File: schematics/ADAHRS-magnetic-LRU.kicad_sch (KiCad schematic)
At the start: 23 parts, among them Q1 2N2222, Q2 IRF7171M, Q3 Q2 - 2N2907, Q4 2N2222, Q5 IRF7171M, U2 AD8421TRMZ-EP, U3 AD8421TRMZ-EP

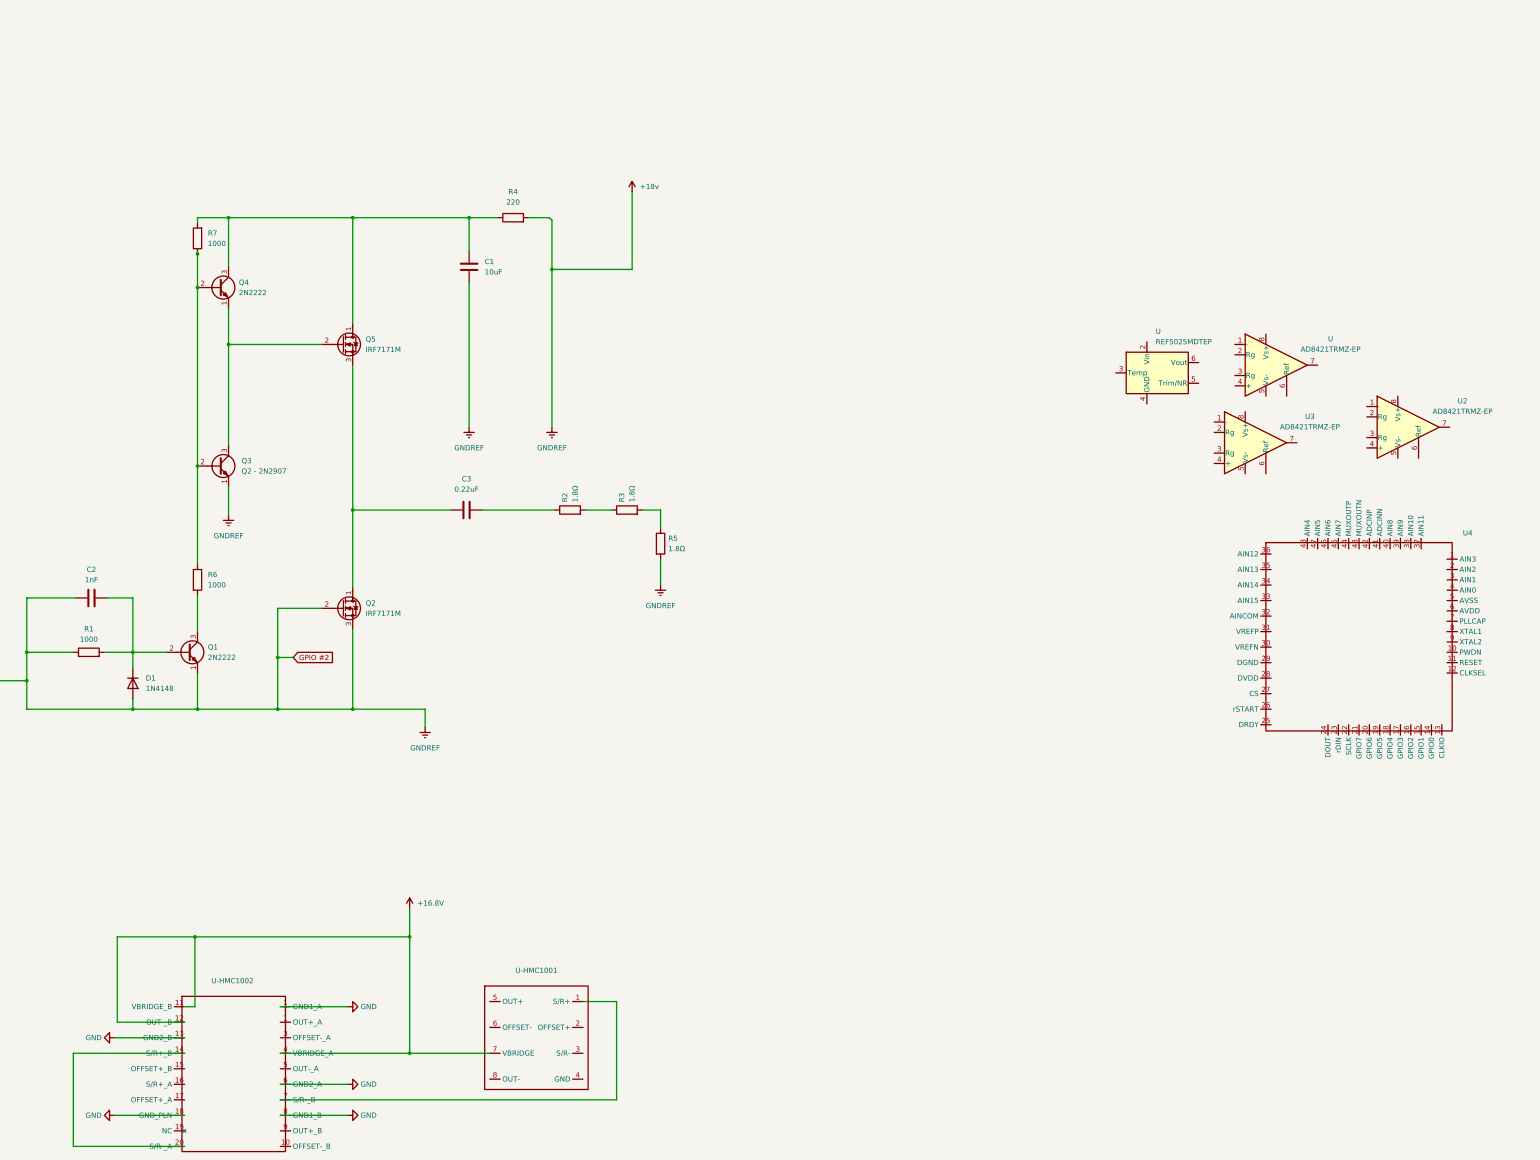
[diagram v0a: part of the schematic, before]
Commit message: rough draft of magnetometer v1_02
I still need to double check and try to clean up as best as possible
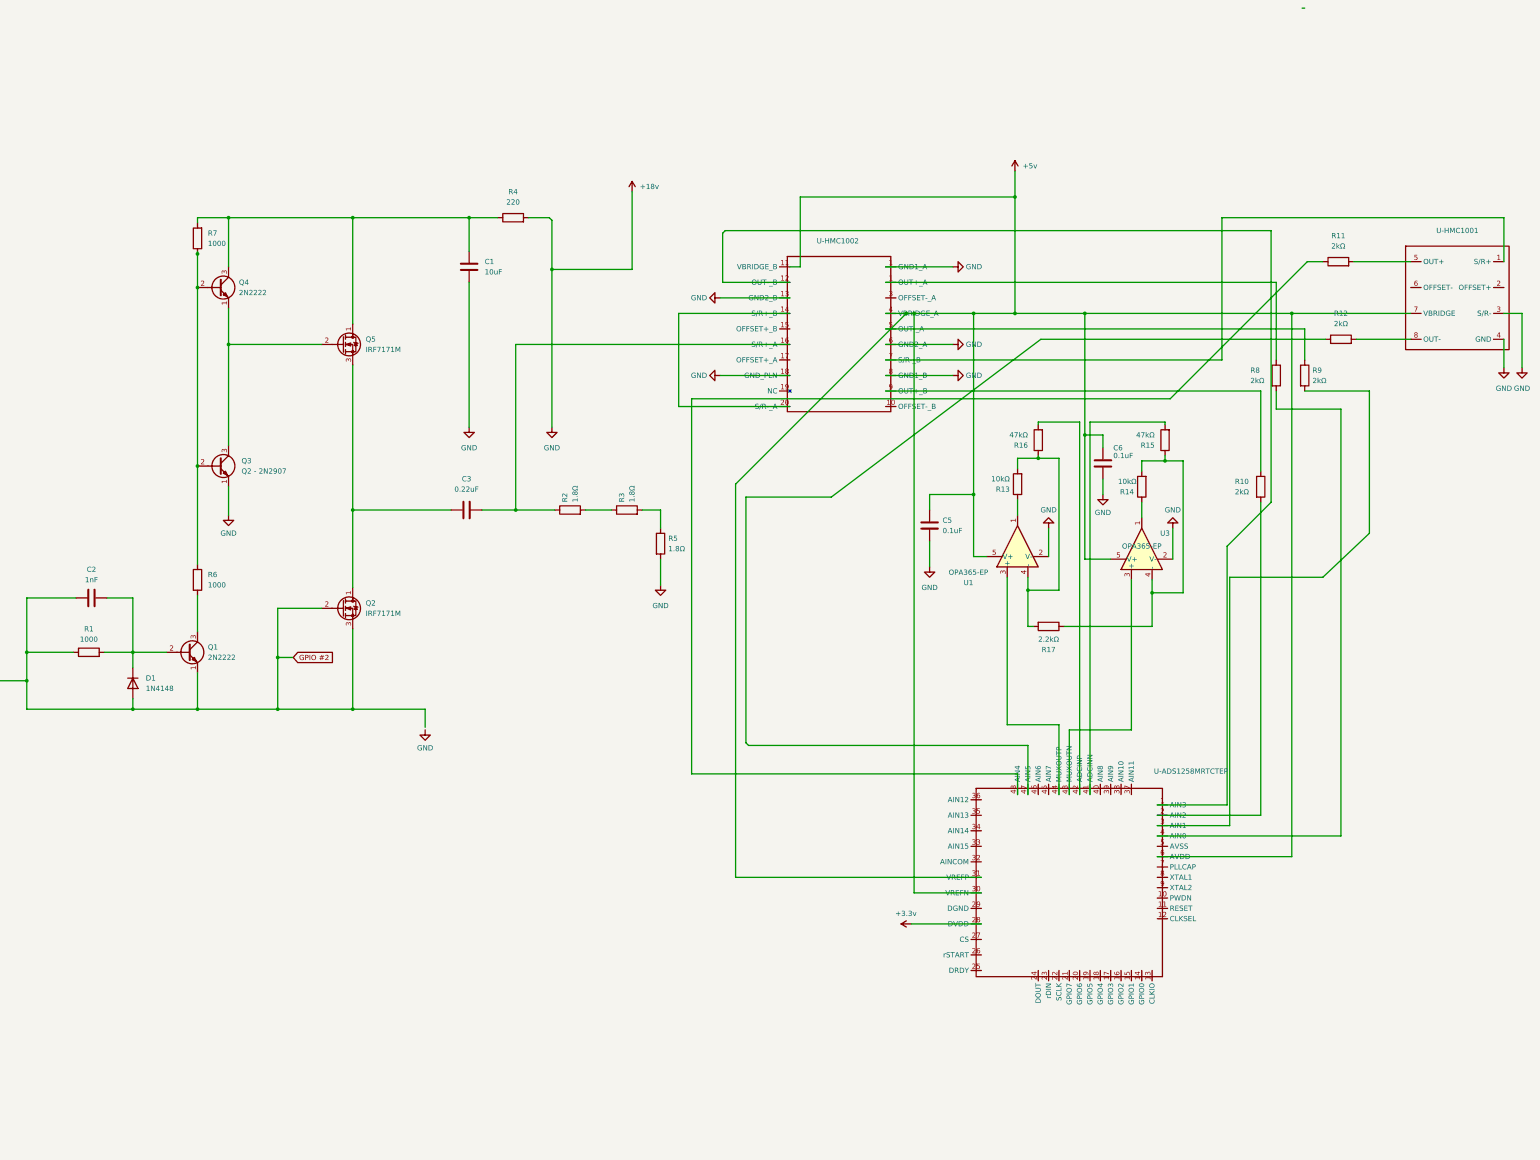
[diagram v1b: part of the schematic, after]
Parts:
- removed U: REF5025MDTEP, Package_SO:SOIC-8_3.9x4.9mm_P1.27mm, symbol Reference_Voltage:REF5025AD
- removed U, U2, U3: AD8421TRMZ-EP, symbol Amplifier_Instrumentation:AD8421
- added C5, C6: 0.1uF, symbol Device:C
- added R10, R11, R12, R8, R9: 2kΩ, symbol Device:R
- added R13, R14: 10kΩ, symbol Device:R
- added R15, R16: 47kΩ, symbol Device:R
- added R17: 2.2kΩ, symbol Device:R
- added U1, U3: OPA365-EP, Package_TO_SOT_SMD:SOT-23-5, symbol Amplifier_Operational:OPA365xxDBV
- renumbered U4 to U-ADS1258MRTCTEP
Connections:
- net GND is gone; now on net +18v: U-HMC1002.1 (OUT+_A), U-HMC1002.13 (GND2_B), U-HMC1002.18 (GND_PLN), U-HMC1002.6 (GND2_A), U-HMC1002.8 (GND1_B)
- net +18v: now also U-HMC1001.3 (S/R-), U-HMC1001.4 (GND), C5.2, C6.2, U1.2 (V-), U3.2 (V-); no longer C2.1, D1.2 (A), Q1.1 (E), Q2.2 (G), Q2.3 (S), R1.1
- net at U-ADS1258MRTCTEP.1 (AIN3): now also U-HMC1002.12 (OUT-_B)
- net at U-ADS1258MRTCTEP.2 (AIN2): now also R10.2
- net +3.3v: now reaches U-ADS1258MRTCTEP.28 (DVDD)
- net at U-ADS1258MRTCTEP.3 (AIN1): now also R9.2
- net +5v: now reaches U-ADS1258MRTCTEP.30 (VREFN)
- net +5v: now also U-ADS1258MRTCTEP.31 (VREFP), U-ADS1258MRTCTEP.6 (AVDD), U-HMC1001.7 (VBRIDGE), U-HMC1002.11 (VBRIDGE_B), U-HMC1002.4 (VBRIDGE_A), C5.1, C6.1, U1.5 (V+), U3.5 (V+)
- net at U-ADS1258MRTCTEP.4 (AIN0): now also R8.2
- net at U-ADS1258MRTCTEP.41 (ADCINN): now also R15.2
- net at U-ADS1258MRTCTEP.42 (ADCINP): now also R16.2
- net at U-ADS1258MRTCTEP.43 (MUXOUTN): now also U3.3 (+)
- net at U-ADS1258MRTCTEP.44 (MUXOUTP): now also U1.3 (+)
- net at U-ADS1258MRTCTEP.47 (AIN5): now also R12.1
- net at U-ADS1258MRTCTEP.48 (AIN4): now also R11.1
- net at U-HMC1001.5 (OUT+): now also R11.2
- net at U-HMC1001.8 (OUT-): now also R12.2
- net at U-HMC1002.16 (S/R+_A): now also C3.2, R2.1
- net at U-HMC1002.5 (OUT-_A): now also R9.1
- net at U-HMC1002.9 (OUT+_B): now also R10.1
- removed net +16.8V: U-HMC1001.7 (VBRIDGE), U-HMC1002.11 (VBRIDGE_B), U-HMC1002.12 (OUT-_B), U-HMC1002.4 (VBRIDGE_A)
- new net: R14.2, R15.1, R17.1, U3.4 (-)
- new net: R13.2, R16.1, R17.2, U1.4 (-)
- new net: R8.1, U-HMC1002.1 (OUT+_A)
- new net: R14.1, U3.1
- new net: R13.1, U1.1
- new net GPIO #1: C2.1, D1.2 (A), Q1.1 (E), Q2.2 (G), Q2.3 (S), R1.1
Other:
- moved on the sheet: U-ADS1258MRTCTEP, U-HMC1001, U-HMC1002

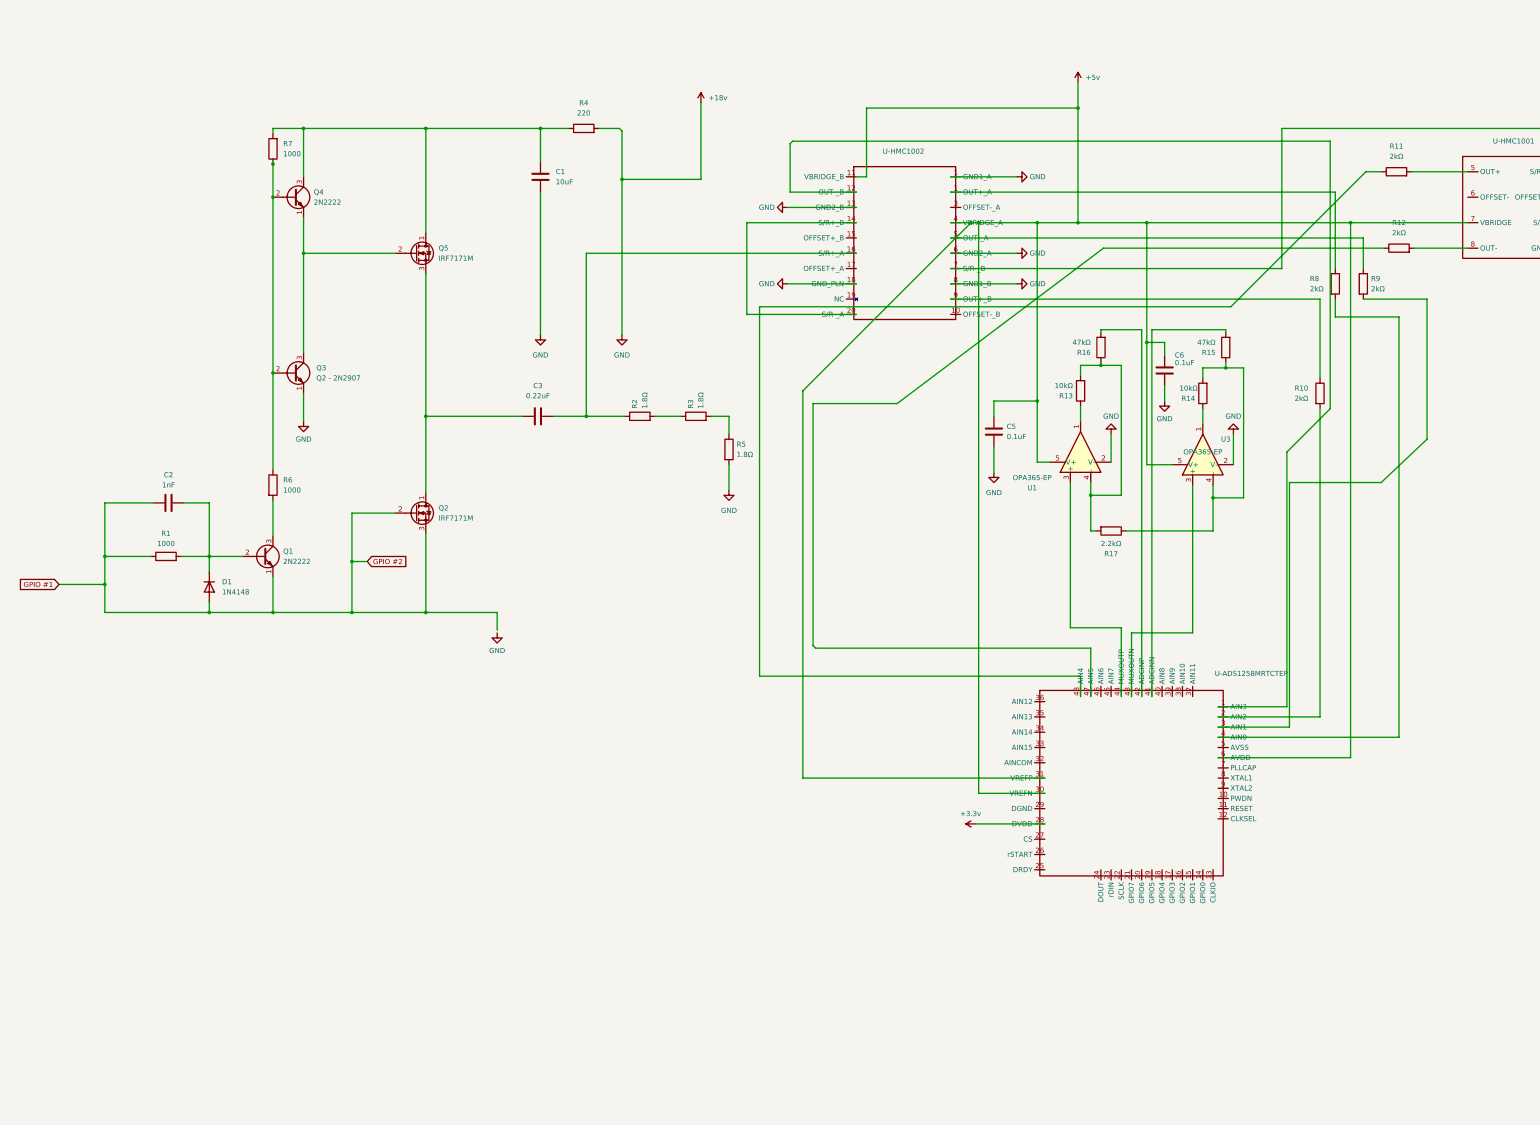
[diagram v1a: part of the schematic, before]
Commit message: v1_03
I cleaned up the wiring and checked for accidents in wiring for each major area of the schematic. I still need to check if I wired the power rails correctly to each component and I still need to add RFI filters after the resistors that are 2kΩ which are the wires that connect the output of the HMC1D01 and HMC1D02.
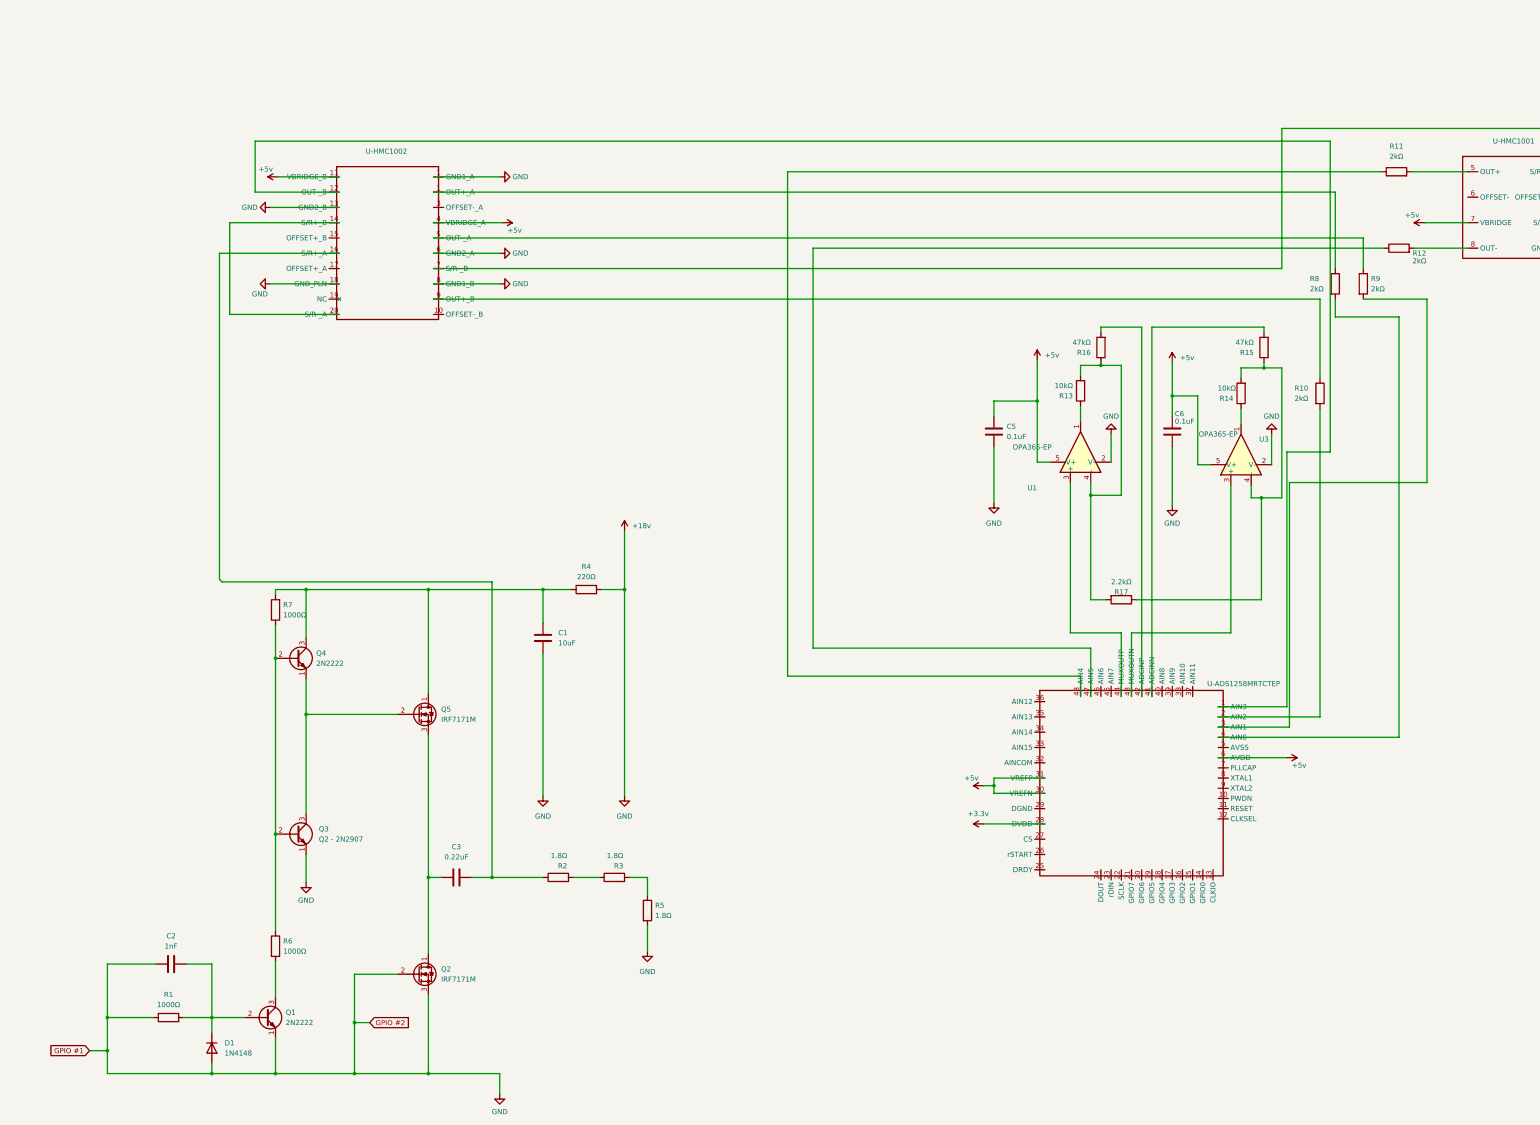
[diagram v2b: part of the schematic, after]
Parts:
- R1, R6, R7: value 1000 -> 1000Ω
- R4: value 220 -> 220Ω
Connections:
- net GPIO #1 is gone; now on net +18v: C2.1, D1.2 (A), Q1.1 (E), Q2.2 (G), Q2.3 (S), R1.1
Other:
- moved on the sheet: C1, C2, C3, C6, D1, Q1, Q2, Q3, Q4, Q5, R1, R14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

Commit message: Added caps to each power rail
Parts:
- added C10, C11, C12, C4, C7, C8, C9: 0.1uF, symbol Device:C
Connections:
- net +18v: now also C10.1, C11.1, C12.1, C4.1, C7.1, C8.1, C9.1
- net +3.3v: now also C10.2
- net +5v: now also C11.2, C12.2, C4.2, C7.2, C8.2, C9.2
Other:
- moved on the sheet: R2, R3, R5
